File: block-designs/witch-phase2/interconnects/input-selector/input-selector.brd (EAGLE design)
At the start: 99.1 x 66.7 mm, 37 parts, among them IC1 74LVC1G17DBV, IC10 74LVC1G17DBV, IC11 74LVC1G17DBV, IC12 74LVC1G17DBV, IC13 74LVC1G17DBV, IC14 74LVC1G17DBV, IC2 74LVC1G17DBV, IC3 74LVC1G17DBV, IC4 74LVC1G17DBV, IC5 74LVC1G17DBV, IC6 74LVC1G17DBV, IC7 74LVC1G17DBV, IC8 74LVC1G17DBV, IC9 74LVC1G17DBV

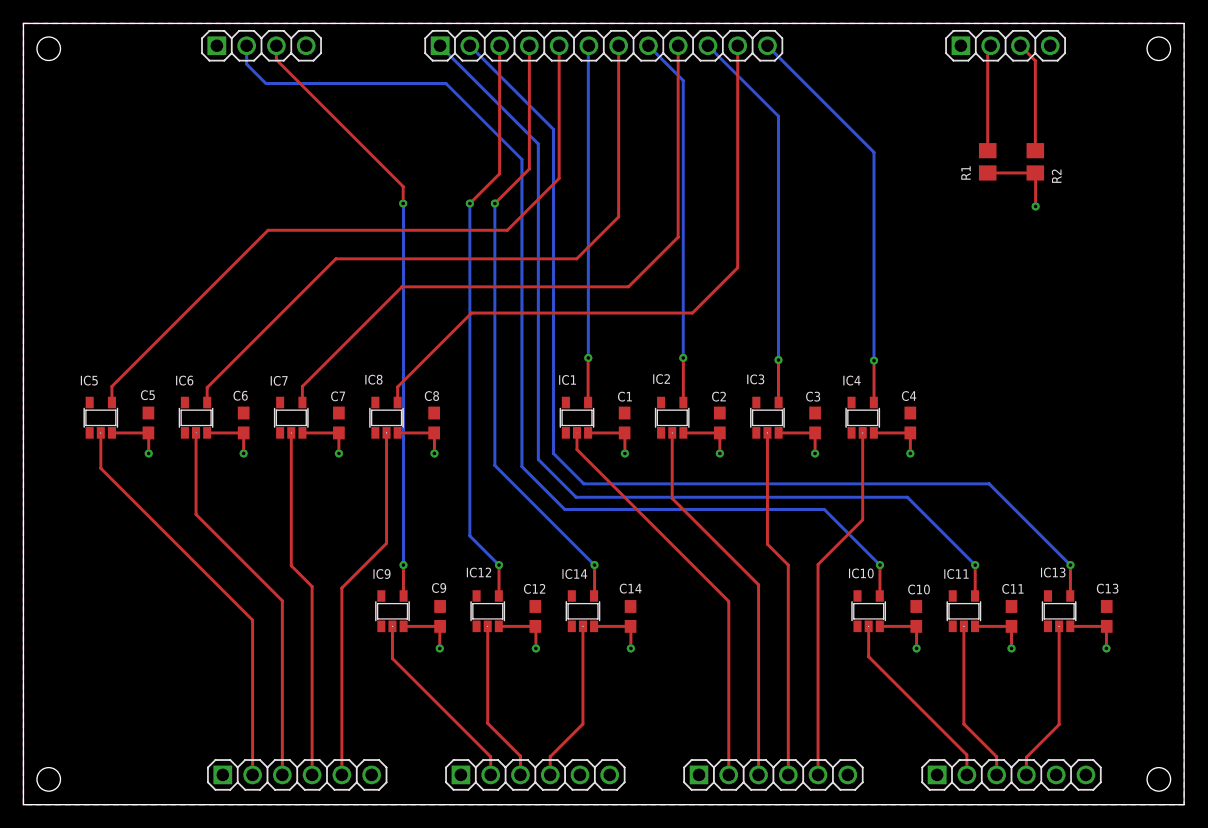
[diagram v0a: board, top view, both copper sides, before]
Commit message: schematic cleanup and change bypass caps from 0805 to 0603
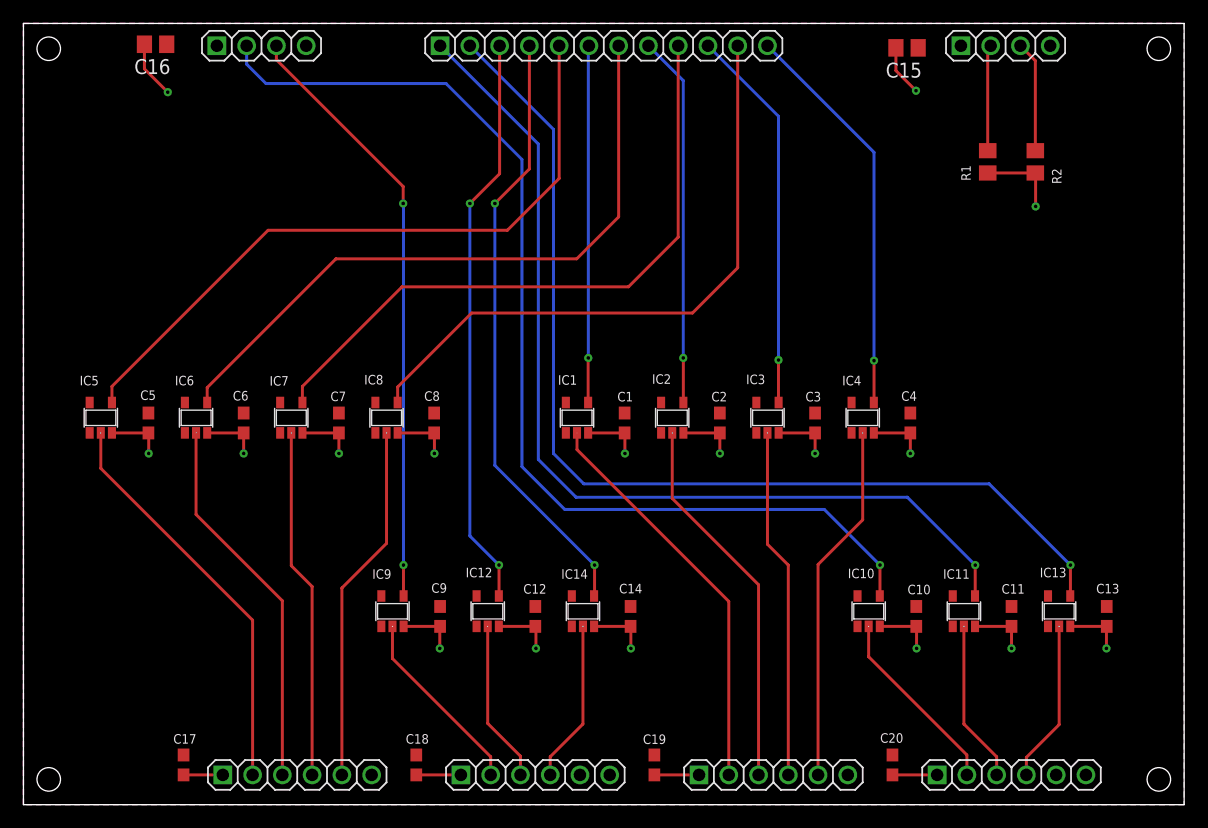
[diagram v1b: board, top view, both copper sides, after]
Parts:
- added C15, C16: (no value), resistor:C0805
- added C17, C18, C19, C20: (no value), resistor:C0603
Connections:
- net GND: now also C15.2, C16.2, C17.2, C18.2, C19.2, C20.2
- net VCC: now also C15.1, C16.1, C17.1, C18.1, C19.1, C20.1
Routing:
- net GND: track 76.0 -> 100.0 mm, vias 15 -> 17
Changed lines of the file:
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@@
 <attribute name="VALUE" x="15.748" y="-0.635" size="1.27" layer="27"/>
+</element>
+<element name="C15" library="resistor" package="C0805" value="" x="75.4126" y="64.5922" rot="R180"/>
+<element name="C16" library="resistor" package="C0805" value="" x="11.2776" y="64.897" rot="R180"/>
+<element name="C17" library="resistor" package="C0603" value="" x="13.6652" y="3.3909" smashed="yes" rot="R270">
+<attribute name="NAME" x="12.7889" y="5.207" size="0.8128" layer="25"/>
+<attribute name="VALUE" x="11.7602" y="4.0259" size="1.27" layer="27" rot="R270"/>
+</element>
+<element name="C18" library="resistor" package="C0603" value="" x="33.528" y="3.3909" smashed="yes" rot="R270">
+<attribute name="NAME" x="32.6263" y="5.207" size="0.8128" layer="25"/>
+<attribute name="VALUE" x="31.623" y="4.0259" size="1.27" layer="27" rot="R270"/>
+</element>
+<element name="C19" library="resistor" package="C0603" value="" x="53.848" y="3.3909" smashed="yes" rot="R270">
+<attribute name="NAME" x="52.8701" y="5.1816" size="0.8128" layer="25"/>
+<attribute name="VALUE" x="51.943" y="4.0259" size="1.27" layer="27" rot="R270"/>
+</element>
+<element name="C20" library="resistor" package="C0603" value="" x="74.168" y="3.3909" smashed="yes" rot="R270">
+<attribute name="NAME" x="73.1139" y="5.2832" size="0.8128" layer="25"/>
+<attribute name="VALUE" x="72.263" y="4.0259" size="1.27" layer="27" rot="R270"/>
 </element>
 </elements>
@@
 <via x="75.692" y="29.972" extent="1-16" drill="0.3048"/>
 <wire x1="86.3854" y1="53.8886" x2="86.3854" y2="51.054" width="0.254" layer="1"/>
+<contactref element="C15" pad="2"/>
+<contactref element="C16" pad="2"/>
+<wire x1="10.3276" y1="64.897" x2="10.3276" y2="62.799" width="0.254" layer="1"/>
+<wire x1="10.3276" y1="62.799" x2="12.319" y2="60.8076" width="0.254" layer="1"/>
+<via x="12.319" y="60.8076" extent="1-16" drill="0.3048"/>
+<wire x1="74.4626" y1="64.5922" x2="74.4626" y2="62.6466" width="0.254" layer="1"/>
+<wire x1="74.4626" y1="62.6466" x2="76.1746" y2="60.9346" width="0.254" layer="1"/>
+<via x="76.1746" y="60.9346" extent="1-16" drill="0.3048"/>
+<contactref element="C17" pad="2"/>
+<contactref element="C18" pad="2"/>
+<contactref element="C19" pad="2"/>
+<contactref element="C20" pad="2"/>
+<wire x1="17.018" y1="2.54" x2="13.6661" y2="2.54" width="0.254" layer="1"/>
+<wire x1="13.6661" y1="2.54" x2="13.6652" y2="2.5409" width="0.254" layer="1"/>
+<wire x1="37.338" y1="2.54" x2="33.5289" y2="2.54" width="0.254" layer="1"/>
+<wire x1="33.5289" y1="2.54" x2="33.528" y2="2.5409" width="0.254" layer="1"/>
+<wire x1="57.658" y1="2.54" x2="53.8489" y2="2.54" width="0.254" layer="1"/>
+<wire x1="53.8489" y1="2.54" x2="53.848" y2="2.5409" width="0.254" layer="1"/>
+<wire x1="77.978" y1="2.54" x2="74.1689" y2="2.54" width="0.254" layer="1"/>
+<wire x1="74.1689" y1="2.54" x2="74.168" y2="2.5409" width="0.254" layer="1"/>
 </signal>
 <signal name="VCC">
@@
 <contactref element="C7" pad="1"/>
 <contactref element="C8" pad="1"/>
+<contactref element="C15" pad="1"/>
+<contactref element="C16" pad="1"/>
+<contactref element="C17" pad="1"/>
+<contactref element="C18" pad="1"/>
+<contactref element="C19" pad="1"/>
+<contactref element="C20" pad="1"/>
 </signal>
 <signal name="SND_ENABLE">

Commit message: add revision numbers
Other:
- board text added: "Revision 1"
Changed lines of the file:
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@@
 <text x="64.008" y="5.588" size="1.778" layer="48" align="center">SND ROW</text>
 <text x="23.368" y="5.588" size="1.778" layer="48" align="center">RCV ROW</text>
-<text x="2.3876" y="56.1086" size="1.778" layer="48">Input Selector Interconnect</text>
+<text x="1.7018" y="51.7144" size="1.778" layer="48">Input Selector
+Interconnect</text>
+<text x="1.7272" y="50.0126" size="0.8128" layer="48">Revision 1</text>
 </plain>
 <attributes>
@@
 <attribute name="VALUE" x="15.748" y="-0.635" size="1.27" layer="27"/>
 </element>
-<element name="C15" library="resistor" package="C0805" value="" x="75.4126" y="64.5922" rot="R180"/>
-<element name="C16" library="resistor" package="C0805" value="" x="11.2776" y="64.897" rot="R180"/>
+<element name="C15" library="resistor" package="C0805" value="" x="75.4126" y="64.5922" smashed="yes" rot="R180">
+<attribute name="NAME" x="77.47" y="63.0936" size="0.8128" layer="25" rot="R180"/>
+<attribute name="VALUE" x="76.6826" y="67.1322" size="1.27" layer="27" rot="R180"/>
+</element>
+<element name="C16" library="resistor" package="C0805" value="" x="11.2776" y="64.897" smashed="yes" rot="R180">
+<attribute name="NAME" x="13.2588" y="63.3984" size="0.8128" layer="25" rot="R180"/>
+<attribute name="VALUE" x="12.5476" y="67.437" size="1.27" layer="27" rot="R180"/>
+</element>
 <element name="C17" library="resistor" package="C0603" value="" x="13.6652" y="3.3909" smashed="yes" rot="R270">
 <attribute name="NAME" x="12.7889" y="5.207" size="0.8128" layer="25"/>
